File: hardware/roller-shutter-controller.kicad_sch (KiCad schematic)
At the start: 36 parts, among them J1 Screw_Terminal_01x06, J2 Screw_Terminal_01x04, J3 Screw_Terminal_01x10, K1 EC2-3NU, Q1 2N7000, Q2 2N7000, Q3 2N7000, U1 TSR_1-24120, U2 TSR_1-2433, U3 WeMos_C3_mini

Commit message: started work on new rev
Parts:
- removed C3: 10uF, Capacitor_SMD:C_1210_3225Metric_Pad1.33x2.70mm_HandSolder, symbol Device:C
- removed L2: 5.6uH, Inductor_SMD:L_TracoPower_TCK-141, symbol Device:L
- added F1: Fuse, symbol Device:Fuse
- added JP1: SolderJumper_2_Open, symbol Jumper:SolderJumper_2_Open
- added U4: ESP32-C3-WROOM-02U, RF_Module:ESP32-C3-WROOM-02U, symbol RF_Module:ESP32-C3-WROOM-02U
- Q1, Q2, Q3: value 2N7000 -> 2N7002; footprint Package_TO_SOT_THT:TO-92_Inline -> Package_TO_SOT_SMD:SOT-23; symbol Transistor_FET:2N7000 -> Transistor_FET:2N7002
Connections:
- net +12V: now also C4.1, U2.1 (Vin), JP1.2 (B)
- net AUTH_LED: now also Q2.1 (G); no longer Q2.2 (G)
- net ENABLE_RELAY: now also Q1.1 (G); no longer Q1.2 (G)
- net GND: now also Q1.2 (S), Q2.2 (S), Q3.2 (S); no longer Q1.1 (S), Q2.1 (S), Q3.1 (S)
- net LED3: now also Q3.1 (G); no longer Q3.2 (G)
- net at C2.1, L1.2, U1.1 (Vin): now also JP1.1 (A)
- net +24V renamed +VIN
- net +VIN: now also F1.2; no longer J1.1 (Pin_1)
- new net: U4.19 (GND), U4.9 (GND)
- new net: F1.1, J1.1 (Pin_1)
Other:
- note added: "Shutter Controller or Power Input"
- note added: "VIN Specification +12V with JP1 shorted +15-36V with JP1 open"
- note removed: "Shutter Controller"
- moved on the sheet: C1, C2, L1, TP1, U1

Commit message: first draft of v4 schematic
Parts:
- removed C5: 10uF, Capacitor_SMD:C_1210_3225Metric_Pad1.33x2.70mm_HandSolder, symbol Device:C
- removed C6: 0.1uF, Capacitor_SMD:C_0603_1608Metric_Pad1.08x0.95mm_HandSolder, symbol Device:C
- removed C7: 1uF, Capacitor_SMD:C_0603_1608Metric_Pad1.08x0.95mm_HandSolder, symbol Device:C
- removed LED1, LED2, LED3: LED, LED_SMD:LED_0603_1608Metric_Pad1.05x0.95mm_HandSolder, symbol Device:LED
- removed R3: 10k, Resistor_SMD:R_0603_1608Metric_Pad0.98x0.95mm_HandSolder, symbol Device:R
- removed R4, R5, R6: 220R, Resistor_SMD:R_0603_1608Metric_Pad0.98x0.95mm_HandSolder, symbol Device:R
- removed U3: WeMos_C3_mini, Lolin C3 Mini:wemos-d1-mini-with-pin-header-and-connector, symbol Custom:WeMos_C3_mini
- removed U4: ESP32-C3-WROOM-02U, RF_Module:ESP32-C3-WROOM-02U, symbol RF_Module:ESP32-C3-WROOM-02U
- added C3: 10uF, Capacitor_SMD:C_1210_3225Metric_Pad1.33x2.70mm_HandSolder, symbol Device:C
- added J6: Screw_Terminal_01x06, symbol Connector:Screw_Terminal_01x06
- added TP3, TP4: TestPoint, TestPoint:TestPoint_Pad_1.0x1.0mm, symbol Connector:TestPoint
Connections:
- net +12V: now also J6.4 (Pin_4)
- net +3V3: now also C3.1, J6.5 (Pin_5)
- net +VIN: now also J6.3 (Pin_3)
- net GND: now also C3.2, J6.6 (Pin_6), TP3.1, TP4.1
- net LOWER: now also J6.2 (Pin_2)
- net RAISE: now also J6.1 (Pin_1)
- net AUTH_LED renamed Microcontroller/AUTH_LED
- net ENABLE_RELAY renamed Microcontroller/ENABLE_RELAY
- net LED3 renamed Microcontroller/LED3
- no-connect marks 3 -> 2
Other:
- added sheet Microcontroller (microcontroller.kicad_sch)
- note added: "Relay Wetting"
- note added: "Wire link required wetting voltage to RAISE and/or LOWER, or connect external supply to RAISE and/or LOWER"
- note removed: "12V Power Supply"
- note removed: "3.3V Power Supply"
- note removed: "Output Relay"
- note removed: "Reserved for OLED Screen"
- note removed: "Screw Terminals"
- note removed: "Wemos C3 Mini"
- moved on the sheet: C1, C2, C4, D1, D2, D3, F1, J1, J2, J3, JP1, K1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

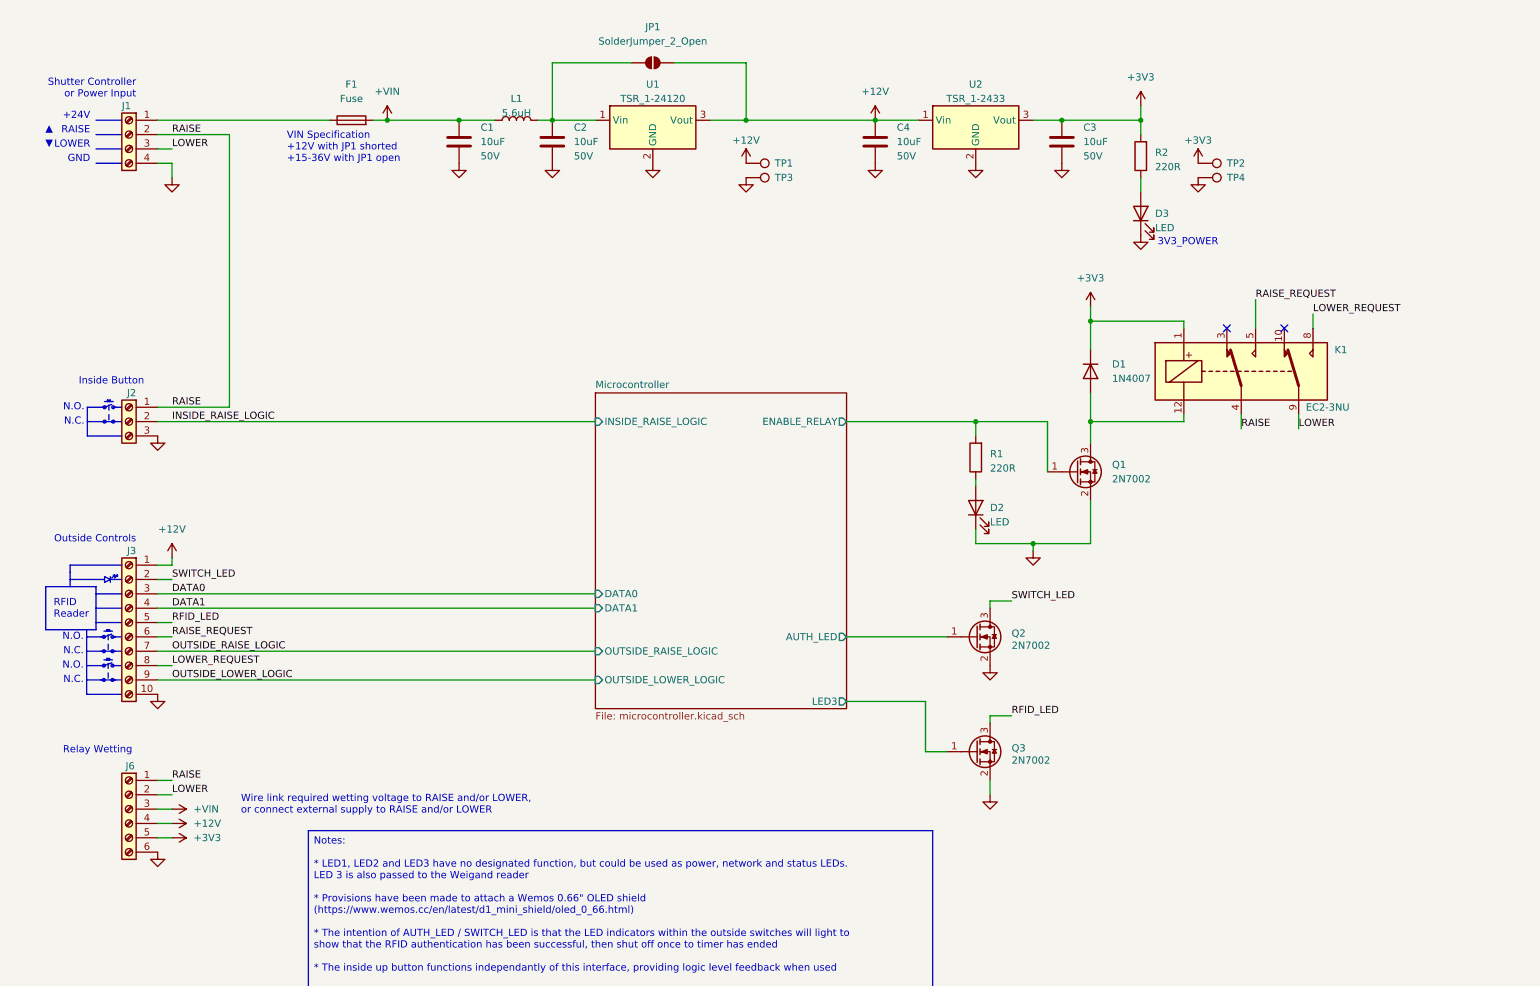
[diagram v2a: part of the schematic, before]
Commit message: swapped DC-DCs, upgraded to S3
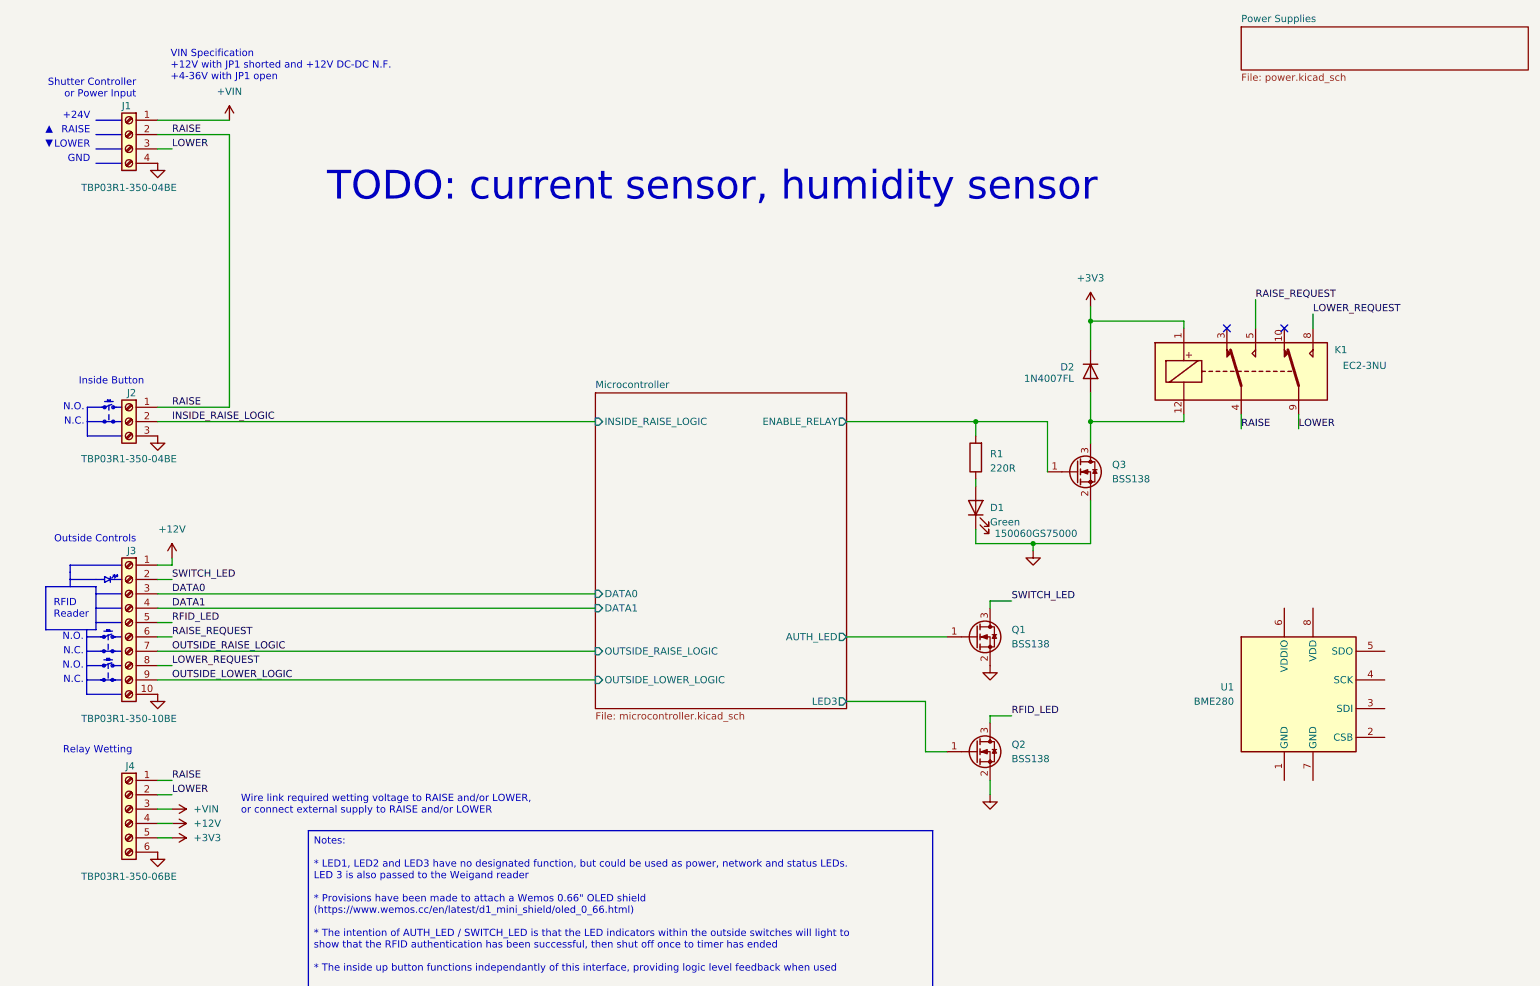
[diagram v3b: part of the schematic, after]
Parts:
- removed C1, C2, C3, C4: 10uF, Capacitor_SMD:C_1210_3225Metric_Pad1.33x2.70mm_HandSolder, symbol Device:C
- removed D3: LED, LED_SMD:LED_0603_1608Metric_Pad1.05x0.95mm_HandSolder, symbol Device:LED
- removed F1: Fuse, symbol Device:Fuse
- removed JP1: SolderJumper_2_Open, symbol Jumper:SolderJumper_2_Open
- removed L1: 5.6uH, Inductor_SMD:L_TracoPower_TCK-141, symbol Device:L
- removed Q1, Q2, Q3: 2N7002, Package_TO_SOT_SMD:SOT-23, symbol Transistor_FET:2N7002
- removed R2: 220R, Resistor_SMD:R_0603_1608Metric_Pad0.98x0.95mm_HandSolder, symbol Device:R
- removed TP1, TP2, TP3, TP4: TestPoint, TestPoint:TestPoint_Pad_1.0x1.0mm, symbol Connector:TestPoint
- removed U1: TSR_1-24120, Converter_DCDC:Converter_DCDC_TRACO_TSR-1_THT, symbol Regulator_Switching:TSR_1-24120
- removed U2: TSR_1-2433, Converter_DCDC:Converter_DCDC_TRACO_TSR-1_THT, symbol Regulator_Switching:TSR_1-2433
- added Q1, Q2, Q3: BSS138, Package_TO_SOT_SMD:SOT-23_Handsoldering, symbol Transistor_FET:BSS138
- added U1: BME280, Package_LGA:Bosch_LGA-8_2.5x2.5mm_P0.65mm_ClockwisePinNumbering, symbol Sensor:BME280
- D1: renamed from D2; value LED -> Green; MPN (none) -> 150060GS75000; Manufacturer (none) -> Wurth; SPN (none) -> 732-4971-1-ND
- D2: renamed from D1; MPN (none) -> 1N4007FL; Manufacturer (none) -> SMC; SPN (none) -> 1655-1N4007FLCT-ND
- J1, J2: MPN (none) -> TBP03R1-350-04BE; Manufacturer (none) -> Same Sky; SPN (none) -> 2223-TBP03R1-350-04BE-ND
- J3: MPN (none) -> TBP03R1-350-10BE; Manufacturer (none) -> Same Sky; SPN (none) -> 2223-TBP03R1-350-10BE-ND
- J4: renamed from J6; MPN (none) -> TBP03R1-350-06BE; Manufacturer (none) -> Same Sky; SPN (none) -> 2223-TBP03R1-350-06BE-ND
- K1: MPN (none) -> EC2-3NU; Manufacturer (none) -> Kemet; SPN (none) -> 399-11042-5-ND
- R1: footprint Resistor_SMD:R_0603_1608Metric_Pad0.98x0.95mm_HandSolder -> Resistor_SMD:R_0402_1005Metric_Pad0.72x0.64mm_HandSolder; Field7 (none) -> 541-4064-1-ND; MPN (none) -> CRCW0402220RFKEDC; Manufacturer (none) -> Vishay
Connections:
- net +VIN: now also J1.1 (Pin_1)
- net GND: now also Q1.2 (S), Q2.2 (S), Q3.2 (S)
- net Microcontroller/AUTH_LED: now also Q1.1 (G)
- net Microcontroller/ENABLE_RELAY: now also Q3.1 (G)
- net Microcontroller/LED3: now also Q2.1 (G)
- net RFID_LED: now also Q2.3 (D)
- net SWITCH_LED: now also Q1.3 (D)
- net at D2.2 (A), K1.12: now also Q3.3 (D)
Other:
- added sheet Power Supplies (power.kicad_sch)
- note added: "TODO: current sensor, humidity sensor"
- note added: "VIN Specification +12V with JP1 shorted and +12V DC-DC N.F. +4-36V with JP1 open"
- note removed: "3V3_POWER"
- note removed: "VIN Specification +12V with JP1 shorted +15-36V with JP1 open"

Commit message: schematic WIP
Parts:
- added BZ?: Buzzer CHECK FOOTPRINT, swap for +12V drive model, Buzzer_Beeper:Buzzer_12x9.5RM7.6, symbol Device:Buzzer
- added Q?: BSS138, Package_TO_SOT_SMD:SOT-23_Handsoldering, symbol Transistor_FET:BSS138
- added U7: ACS724xLCTR-05AB SWAP for TMCS1108A3BQDR, Package_SO:SOIC-8_3.9x4.9mm_P1.27mm, symbol Sensor_Current:ACS724xLCTR-05AB
- D1: DigiKey (none) -> 732-4971-1-ND; SPN 732-4971-1-ND -> (none)
- D2: DigiKey (none) -> 1655-1N4007FLCT-ND; SPN 1655-1N4007FLCT-ND -> (none)
- J1: DigiKey (none) -> 2223-TBP03R1-350-04BE-ND; SPN 2223-TBP03R1-350-04BE-ND -> (none)
- J2: Digikey (none) -> 2223-TBP03R1-350-04BE-ND; SPN 2223-TBP03R1-350-04BE-ND -> (none)
- J3: DigiKey (none) -> 2223-TBP03R1-350-10BE-ND; SPN 2223-TBP03R1-350-10BE-ND -> (none)
- J4: DigiKey (none) -> 2223-TBP03R1-350-06BE-ND; SPN 2223-TBP03R1-350-06BE-ND -> (none)
- K1: DigiKey (none) -> 399-11042-5-ND; SPN 399-11042-5-ND -> (none)
- Q1, Q2, Q3: DigiKey (none) -> BSS138CT-ND; SPN BSS138CT-ND -> (none)
- R1: DigiKey (none) -> 541-4064-1-ND; Field7 541-4064-1-ND -> (none)
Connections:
- net +12V: now also BZ?.1 (+)
- net GND: now also Q?.2 (S)
- new net: U7.1 (IP+), U7.2 (IP+)
- new net: U7.3 (IP-), U7.4 (IP-)
- new net: BZ?.2 (-), Q?.3 (D)
- new net Microcontroller/BUZZER_INT: Q?.1 (G)
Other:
- sheet Microcontroller ports: added BUZZER_INT; removed none
- note added: "TODO: current sensor, buzzer ACS724LLCTR-05AB-T, humidity sensor, RFID reader buzzer"
- note removed: "TODO: current sensor, humidity sensor"

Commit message: wip
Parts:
- U7: value ACS724xLCTR-05AB SWAP for TMCS1108A3BQDR -> TMCS1108A3UQDR
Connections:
- no-connect marks 2 -> 3
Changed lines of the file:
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@@
 	(text "TODO: current sensor, buzzer ACS724LLCTR-05AB-T, humidity sensor, RFID reader buzzer"
 		(exclude_from_sim no)
-		(at -3.81 206.502 0)
+		(at -17.018 225.806 0)
 		(effects
 			(font
@@
 		(diameter 0)
 		(color 0 0 0 0)
+	)
+	(no_connect
+		(at 250.19 111.76)
 	)
 	(no_connect
@@
 			)
 		)
-		(property "Value" "ACS724xLCTR-05AB SWAP for TMCS1108A3BQDR"
+		(property "Value" "TMCS1108A3UQDR"
 			(at 242.1733 99.06 0)
 			(effects
@@
 			)
 		)
-		(property "Datasheet" "http://www.allegromicro.com/~/media/Files/Datasheets/ACS724-Datasheet.ashx?la=en"
+		(property "Datasheet" ""
 			(at 240.03 109.22 0)
 			(effects
@@
 			)
 		)
-		(property "Description" "±5A Bidirectional Hall-Effect Current Sensor, +5.0V supply, 400mV/A, SOIC-8"
+		(property "Description" ""
 			(at 240.03 109.22 0)
 			(effects
